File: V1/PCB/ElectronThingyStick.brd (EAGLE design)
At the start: 100 x 44 mm, 105 parts, among them T2 BC847

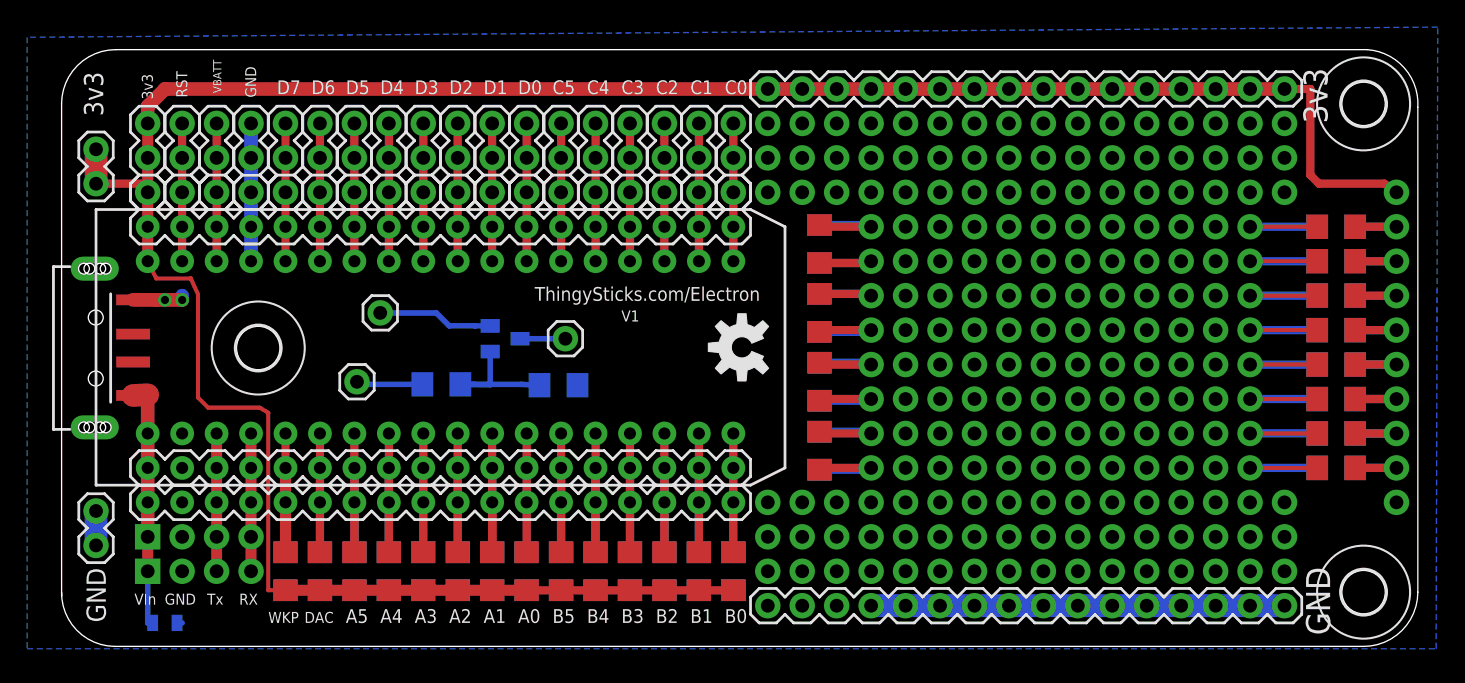
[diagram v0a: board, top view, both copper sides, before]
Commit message: Corrected electron name and minor tidyup.
Added pdfs of the PCB.

Added BOM to list the parts
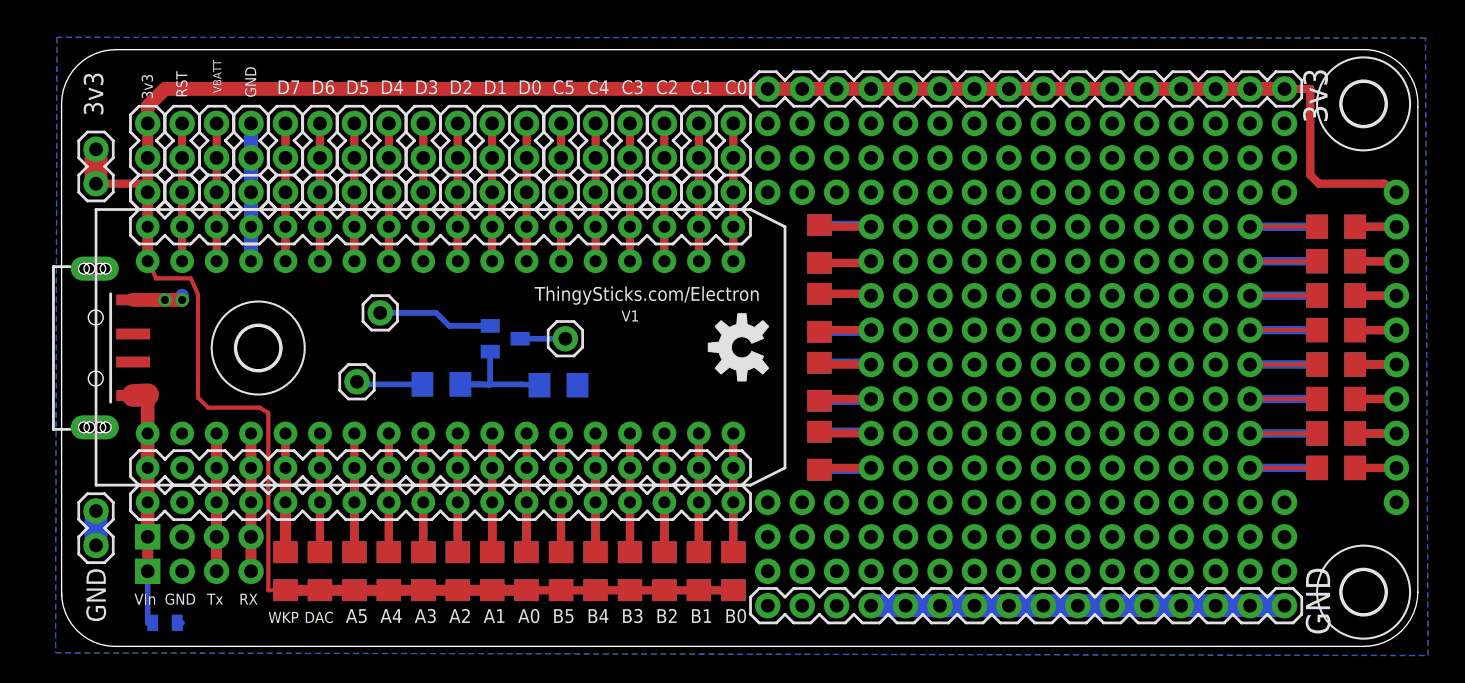
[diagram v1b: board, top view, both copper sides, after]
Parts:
- renumbered U$1 to IC1
